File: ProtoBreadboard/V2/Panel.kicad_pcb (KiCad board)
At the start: 2 copper layers, 121.9 x 172.4 mm, 256 parts, among them IC1 AT90USB1286-AU, IC2 BSS138, IC3 BSS138, IC4 BSS138, IC5 BSS138, J1 Conn_01x30_Female, J10 Conn_01x04_Female, J11 Conn_01x32_Female, J12 Conn_01x06_Female, J13 Conn_01x08_Female, J14 Conn_01x08_Female, J15 Conn_01x04_Female, J16 Conn_01x03_Female, J17 Conn_01x03_Female, J18 Conn_01x07_Female, J19 Conn_01x02_Female, J2 Conn_01x10_Female, J20 Conn_01x02_Female, J21 Conn_01x02_Female, J22 AVR-ISP-6, J23 Conn_01x02_Female, J24 Conn_01x03_Female, J25 Conn_01x07_Female, J26 Conn_01x03_Female, J27 Conn_02x03_Counter_Clockwise, J28 Conn_01x03_Female, J29 Conn_01x02_Female, J3 Conn_01x32_Female, J30 Conn_01x02_Female, J31 Conn_01x02_Female, J32 Conn_01x02_Female, J33 Conn_01x10_Female, J34 Conn_01x10_Female, J35 Conn_01x10_Female, J36 Conn_01x10_Female, J37 Conn_01x10_Female, J38 Conn_01x10_Female, J39 Conn_01x10_Female, J4 Conn_01x10_Female, J40 Conn_01x10_Female, J41 Conn_01x10_Female, J42 Conn_01x10_Female, J43 Conn_01x10_Female, J44 Conn_01x10_Female, J45 Conn_01x10_Female, J46 Conn_01x10_Female, J47 Conn_01x10_Female, J48 Conn_01x10_Female, J49 Conn_01x10_Female, J5 Conn_01x30_Female, J50 Conn_01x10_Female, J51 Conn_01x03_Female, J52 Conn_01x02_Female, J53 Conn_01x04_Female, J54 Conn_01x02_Female, J55 Conn_01x02_Female, J56 Conn_01x02_Female, J57 Conn_01x02_Female, J58 Conn_01x02_Female, J6 Conn_01x02_Female, J7 Conn_01x02_Female, J8 Conn_01x06_Female, J9 Conn_01x04_Female, SW1 RotaryEncoder_Switch, SW2 RotaryEncoder_Switch, U1 IS31FL3741A, U2 AP2112K-3.3, U3 PRTR5V0U2X, U4 AP2112K-3.3, Y1 Crystal, Y2 Crystal, Y3 Crystal

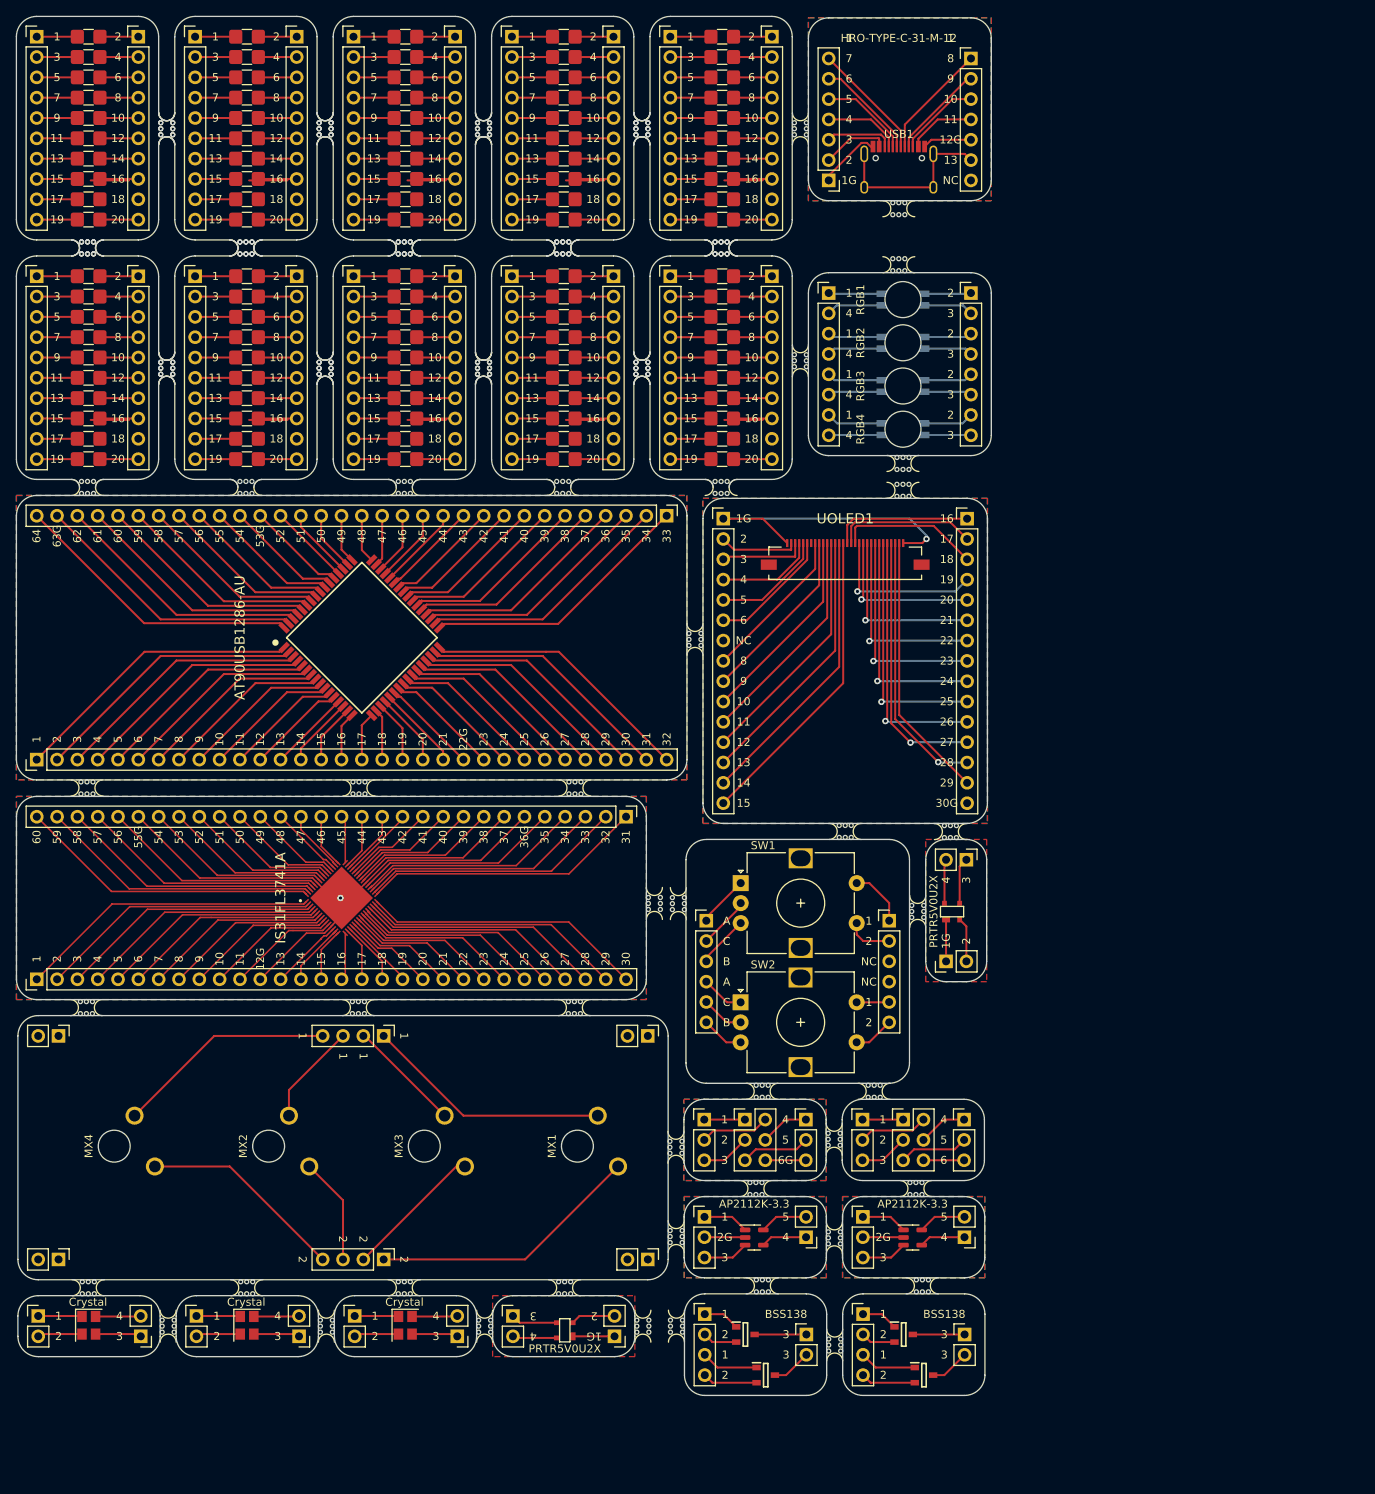
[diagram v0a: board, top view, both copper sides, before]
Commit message: Fixing Edge Cut
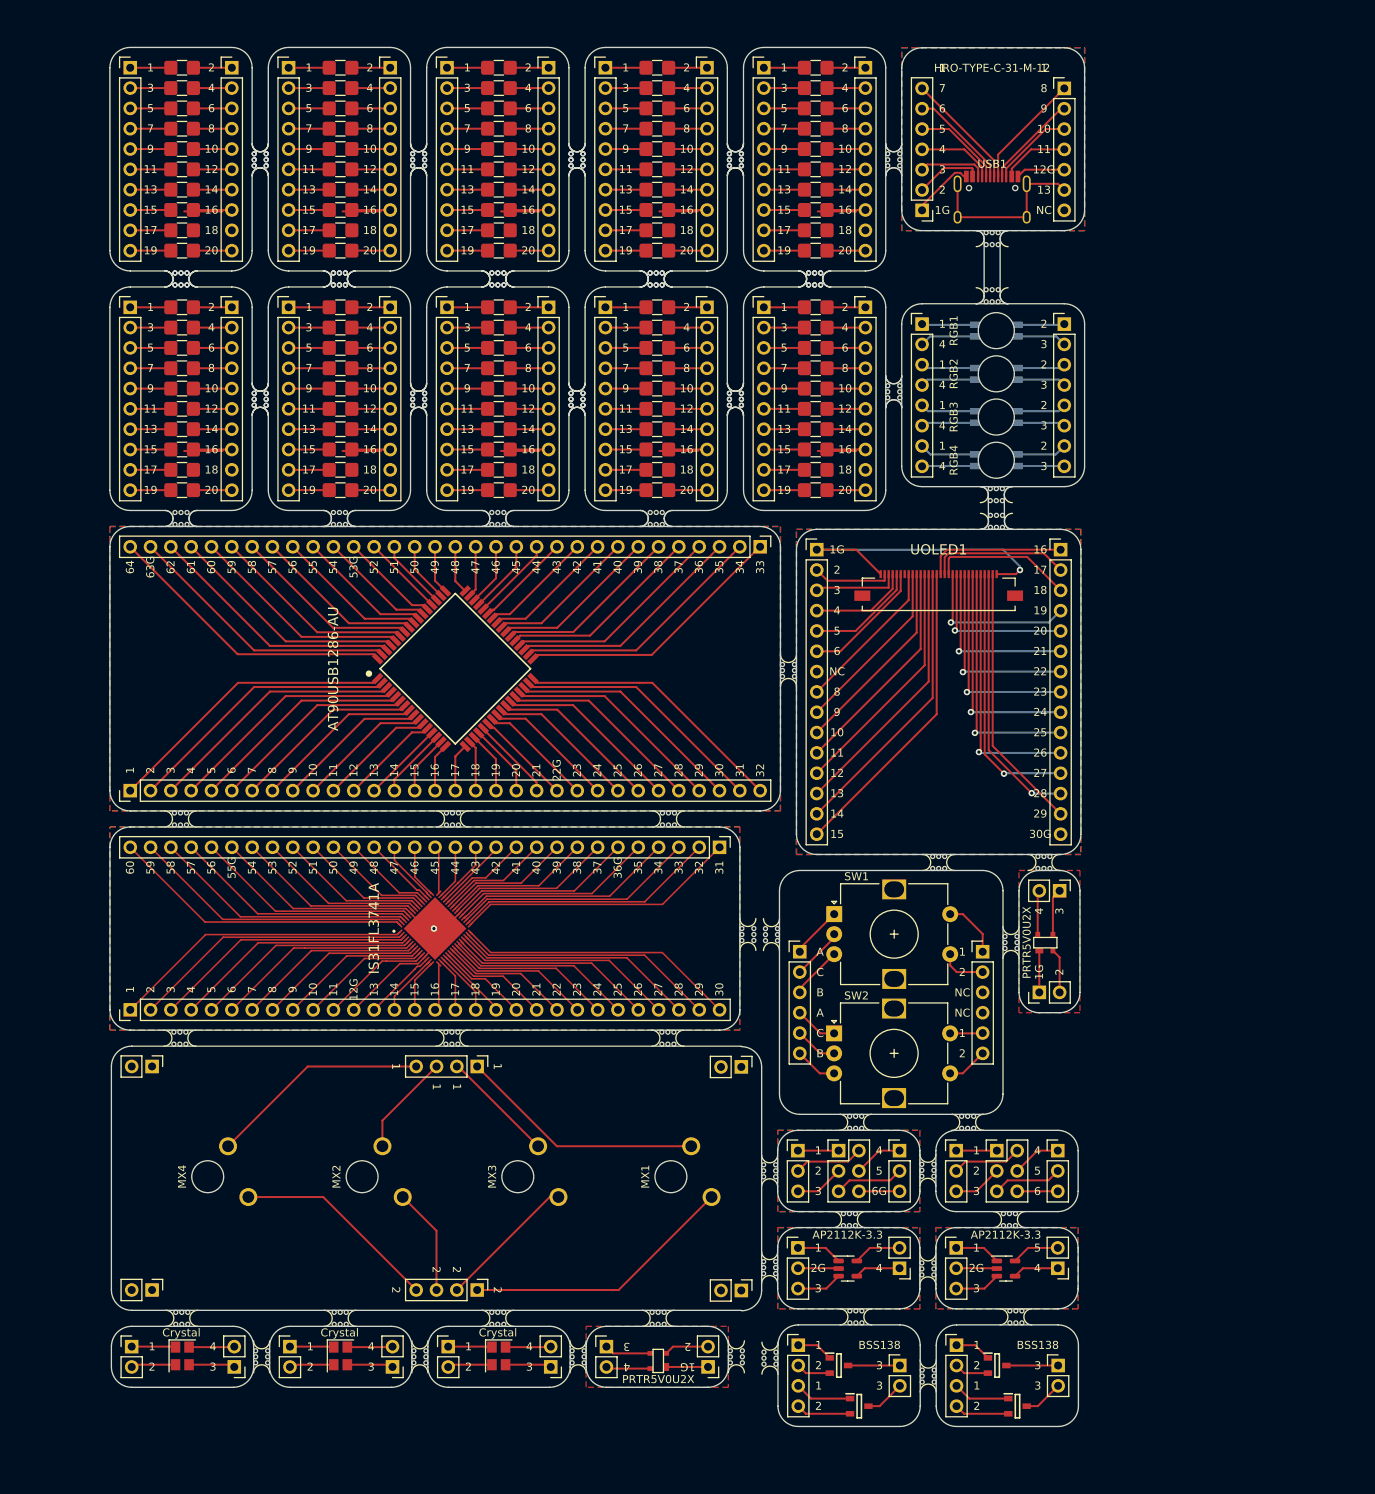
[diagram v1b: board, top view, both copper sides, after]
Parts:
- removed mouse-bite-2mm-slot33: VAL**, Panelization:mouse-bite-2mm-slot
- moved mouse-bite-2mm-slot 12.4 mm to (110.7, 190.6)
- moved J28 12.3 mm to (146.7, 164.7)
- moved J24 12.3 mm to (126.9, 164.7)
- moved J27 12.3 mm to (139.0, 164.7)
- moved mouse-bite-2mm-slot 12.3 mm to (130.4, 167.1)
- moved J17 12.3 mm to (114.2, 164.7)
- moved J22 12.3 mm to (119.3, 164.7)
- moved J26 12.3 mm to (134.0, 164.7)
- moved G31 12.3 mm to (96.6, 29.3)
- moved G35 12.3 mm to (96.6, 39.5)
- moved G36 12.3 mm to (96.6, 42.0)
- moved G37 12.3 mm to (96.6, 44.5)
- moved G84 12.3 mm to (96.6, 66.9)
- moved G86 12.3 mm to (96.6, 71.9)
- moved G87 12.3 mm to (96.6, 74.5)
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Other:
- board size 121.9 x 172.4 mm -> 121.8 x 172.4 mm

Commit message: Completed Mouse bits
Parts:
- moved mouse-bite-2mm-slot 12.3 mm to (123.2, 137.2)
- moved J13 12.3 mm to (142.0, 60.9)
- moved J14 12.3 mm to (159.8, 60.9)
- moved J18 12.3 mm to (142.0, 46.7)
- moved J19 12.3 mm to (156.6, 144.5)
- moved J25 12.3 mm to (159.8, 31.5)
- moved J52 12.3 mm to (159.0, 178.9)
- moved J53 12.3 mm to (146.3, 188.6)
- moved RGB1 12.3 mm to (151.3, 61.7)
- moved RGB2 12.3 mm to (151.3, 67.1)
- moved RGB4 12.3 mm to (151.3, 77.9)
- moved U3 12.3 mm to (157.4, 138.2)
- moved RGB3 12.3 mm to (151.3, 72.5)
- moved mouse-bite-2mm-slot 12.3 mm to (151.3, 82.2)
- moved G11 12.3 mm to (69.3, 28.9)
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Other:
- outline, holes or cut-outs redrawn

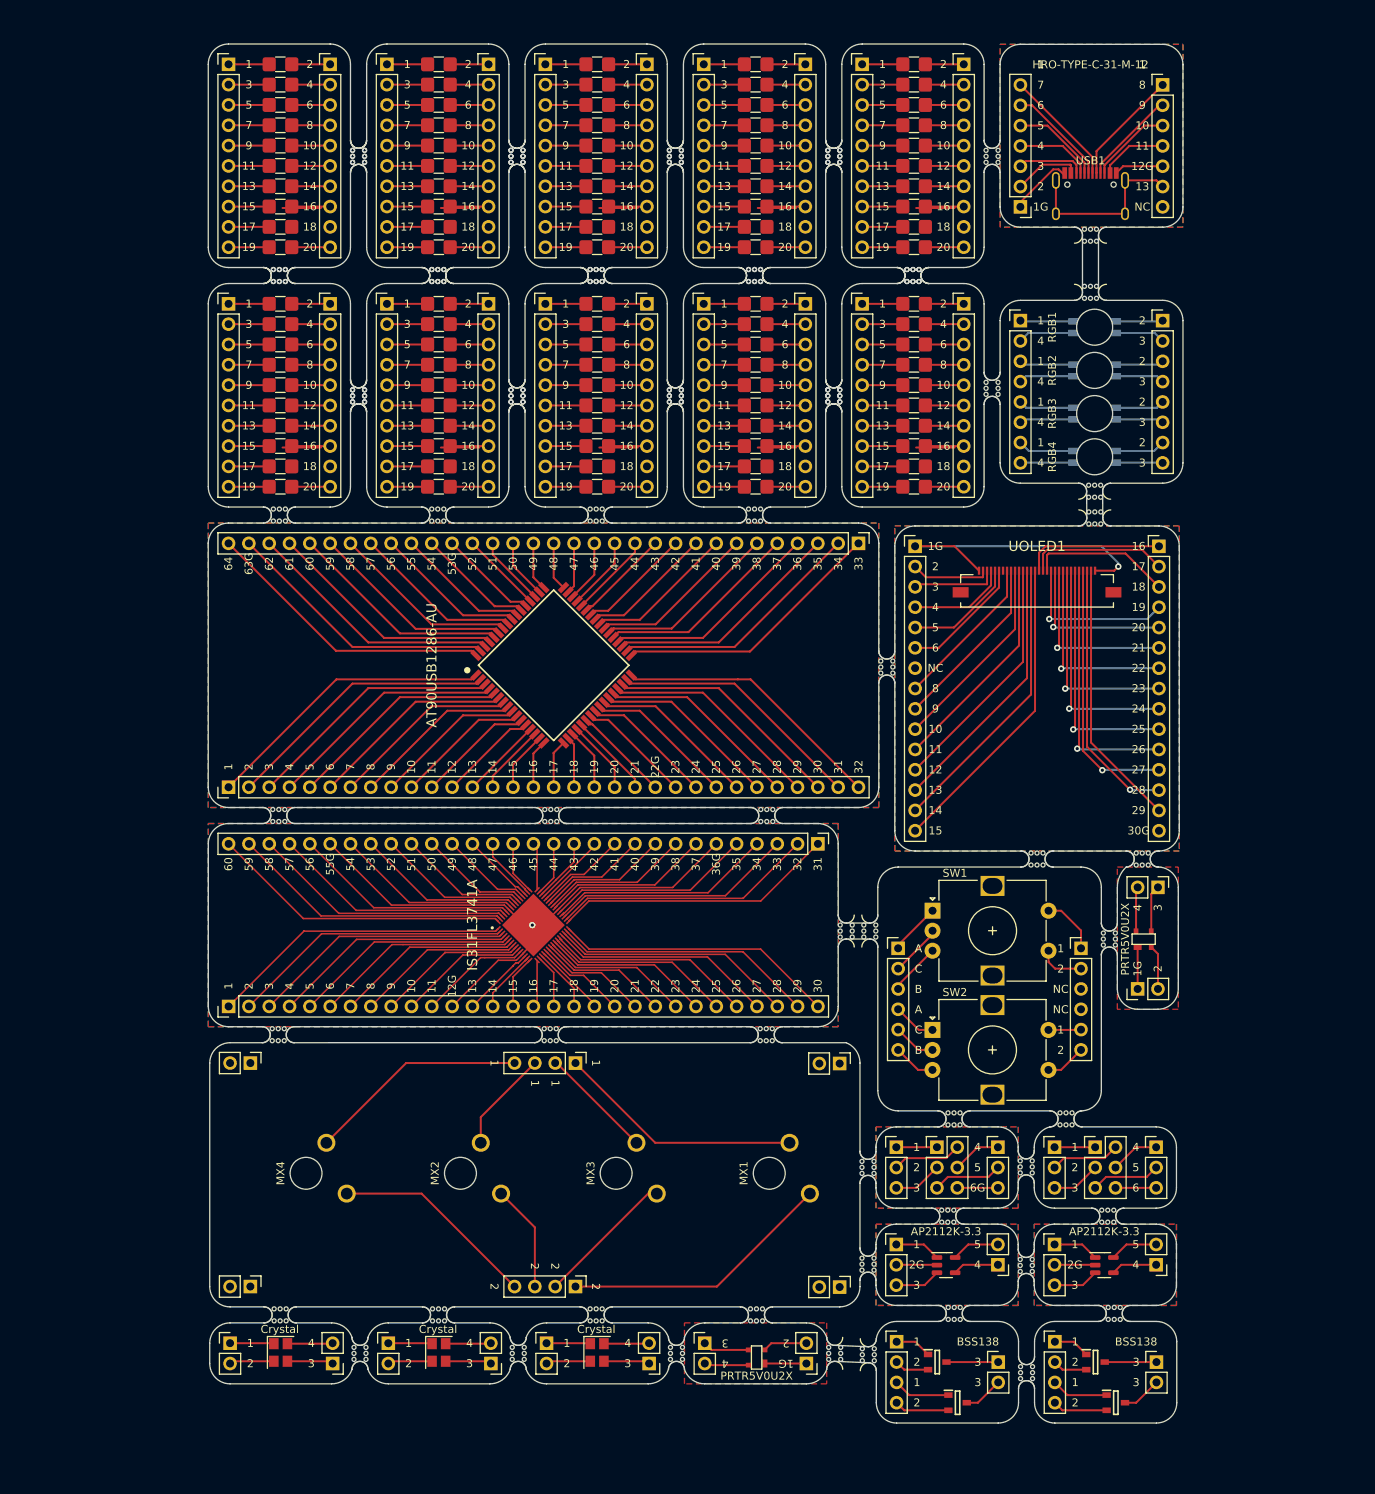
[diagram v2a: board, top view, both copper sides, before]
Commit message: Added one sided mouse bits
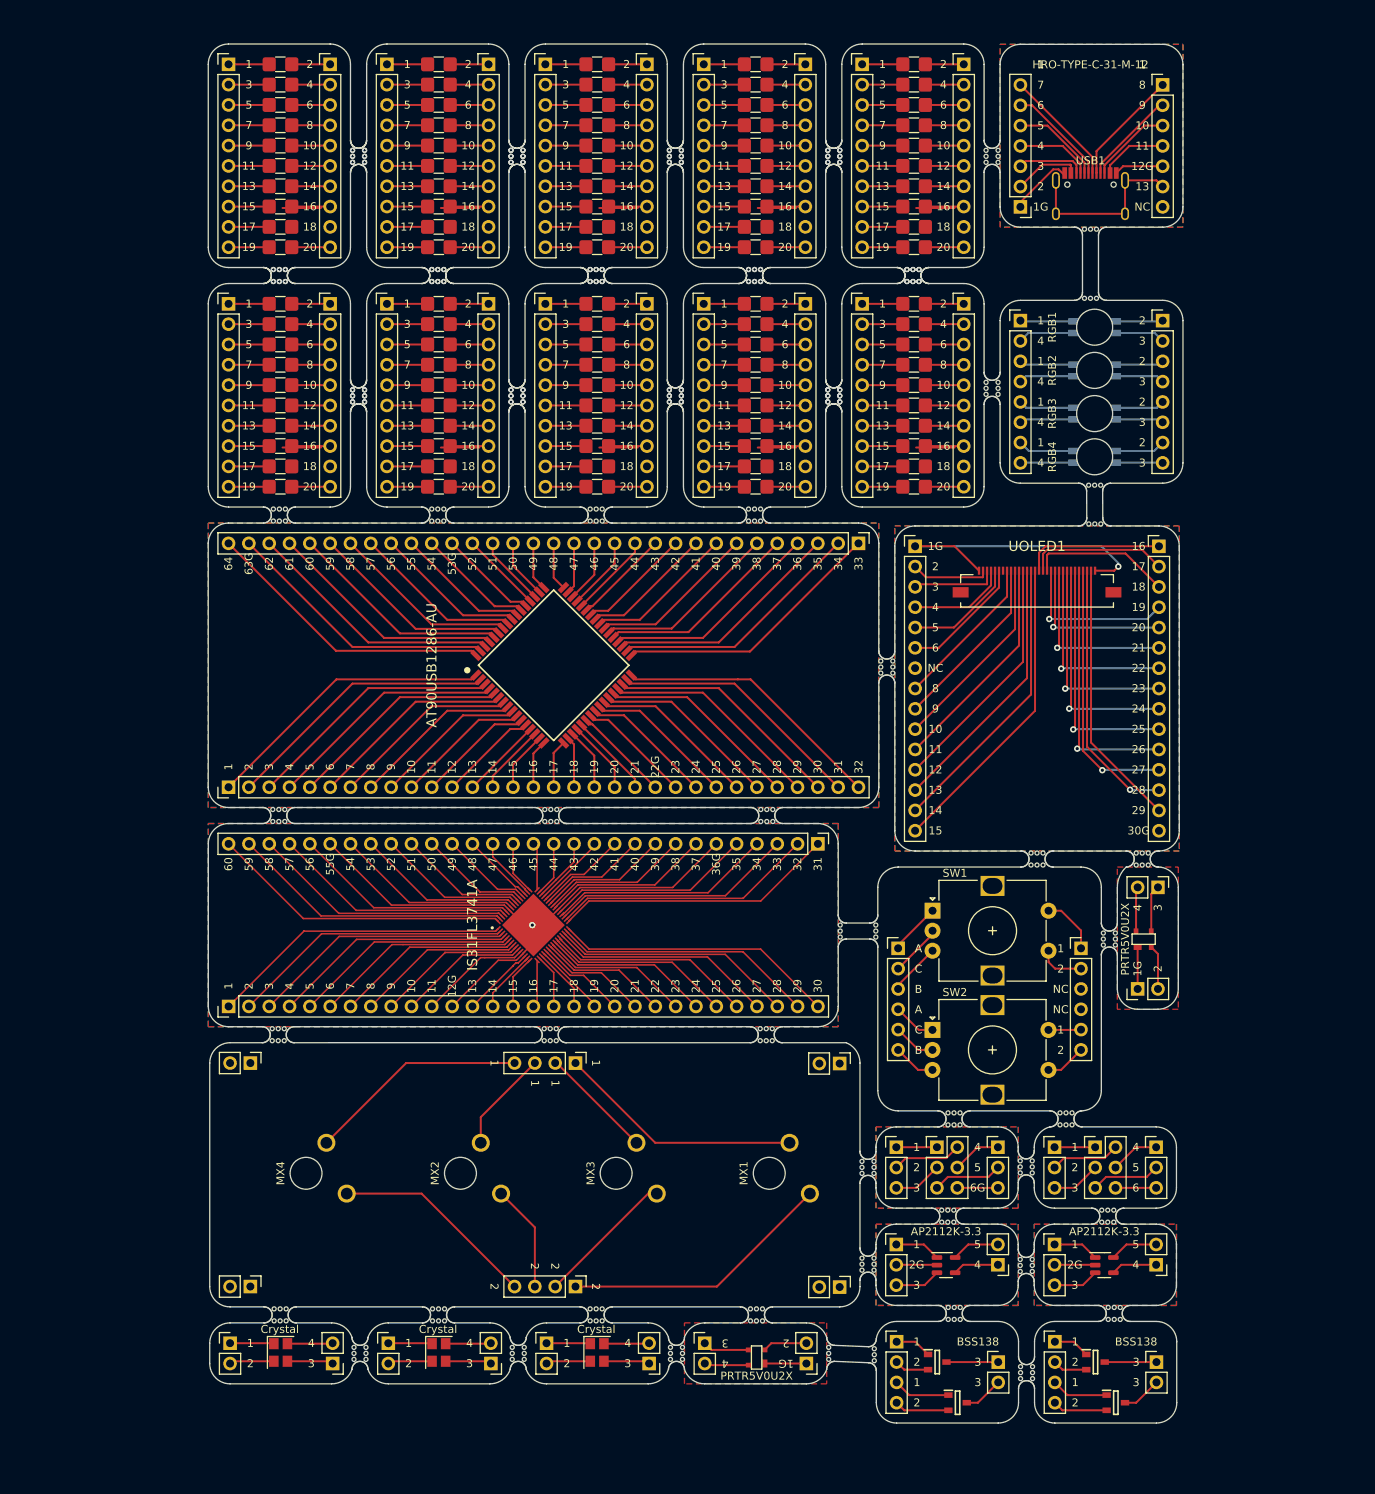
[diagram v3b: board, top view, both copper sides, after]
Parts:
- removed the mouse-bite-2mm-slot at (123.0, 190.2)
- removed the mouse-bite-2mm-slot at (120.2, 137.2)
- removed the mouse-bite-2mm-slot at (123.2, 137.2)
- removed the mouse-bite-2mm-slot at (151.3, 82.2)
- removed the mouse-bite-2mm-slot at (118.8, 190.0)
- removed the mouse-bite-2mm-slot at (151.3, 85.6)
- removed the mouse-bite-2mm-slot14 at (150.8, 50.2)
- removed the mouse-bite-2mm-slot14 at (150.8, 57.4)
- added mouse-bite-2mm-slot: VAL**, Panelization:mouse-bite-2mm-slot-1-side, F.Cu at (150.8, 57.4)
- added mouse-bite-2mm-slot: VAL**, Panelization:mouse-bite-2mm-slot-1-side, F.Cu at (123.2, 137.2)
- added mouse-bite-2mm-slot: VAL**, Panelization:mouse-bite-2mm-slot-1-side, F.Cu at (118.8, 190.0)
- added mouse-bite-2mm-slot: VAL**, Panelization:mouse-bite-2mm-slot-1-side, F.Cu at (123.0, 190.2)
- added mouse-bite-2mm-slot: VAL**, Panelization:mouse-bite-2mm-slot-1-side, F.Cu at (151.3, 85.6)
- added mouse-bite-2mm-slot: VAL**, Panelization:mouse-bite-2mm-slot-1-side, F.Cu at (150.8, 50.2)
- added mouse-bite-2mm-slot: VAL**, Panelization:mouse-bite-2mm-slot-1-side, F.Cu at (120.2, 137.2)
- added mouse-bite-2mm-slot: VAL**, Panelization:mouse-bite-2mm-slot-1-side, F.Cu at (151.3, 82.2)
